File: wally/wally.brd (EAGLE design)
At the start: 5 x 8.6 mm, 28 parts, among them IC1 ESP32-S3-WROOM-1-N4, IC2 XTLV61048DBVR, J6 USBC, U1 RA-01H

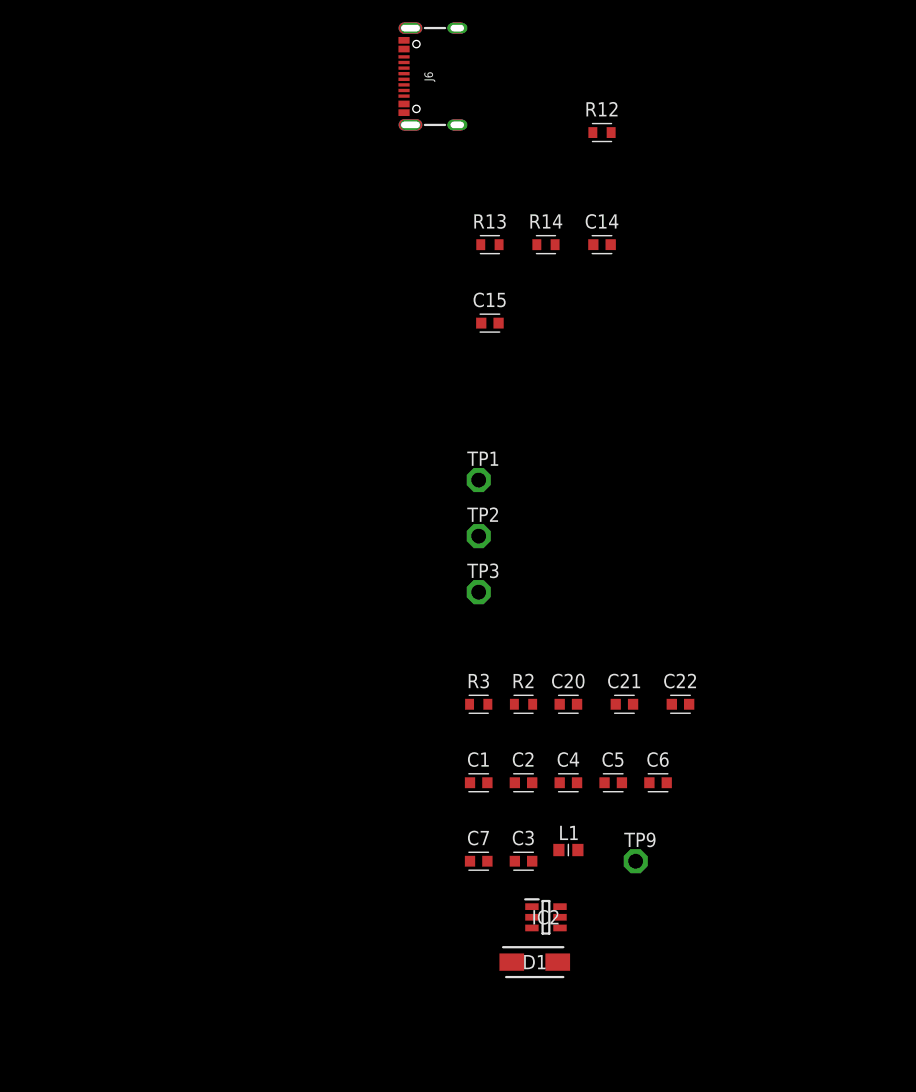
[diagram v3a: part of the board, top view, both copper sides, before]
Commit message: battery inputs
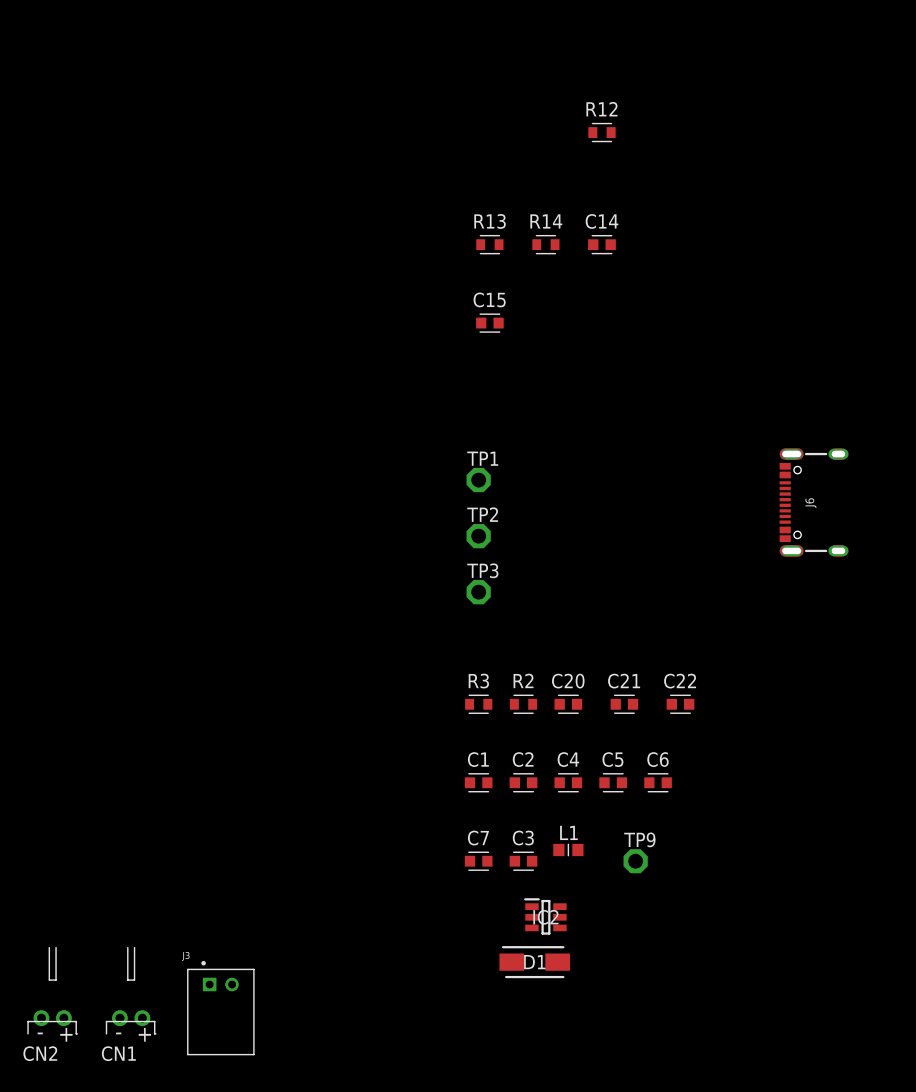
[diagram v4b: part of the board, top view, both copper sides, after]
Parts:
- added CN1, CN2: (no value), adafruit:JST-PH-2-THM-RA
- added J3: S2B-PH-K-S(LF)(SN), Connectors:S2B-PH-K-S(LF)(SN)
- moved J6 51.0 mm to (-24.0, -49.0)
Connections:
- net GND: now also CN1.2, CN2.2
- net VCC: now also CN1.1, CN2.1
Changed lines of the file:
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@@
 <wire x1="0" y1="0" x2="37" y2="0" width="0.254" layer="49"/>
 <wire x1="0" y1="0" x2="0" y2="-100" width="0.254" layer="49"/>
-<wire x1="37" y1="0" x2="36" y2="-1" width="0.254" layer="49"/>
-<wire x1="36" y1="-1" x2="36" y2="-100" width="0.254" layer="49"/>
-<wire x1="36" y1="-100" x2="0" y2="-100" width="0.254" layer="49"/>
+<wire x1="37" y1="0" x2="37" y2="-100" width="0.254" layer="49"/>
+<wire x1="37" y1="-100" x2="0" y2="-100" width="0.254" layer="49"/>
 </plain>
 <attributes>
@@
 <attribute name="VALUE" x="15" y="-67" size="1.27" layer="27" rot="R90" align="center"/>
 </element>
-<element name="J6" library="SparkFun-Connectors" package="USB-C-16P-2LAYER-PADS" override_package3d_urn="urn:adsk.eagle:package:44095805/2" override_package_urn="urn:adsk.eagle:footprint:44095806/1" value="USBC" x="-58" y="-11" smashed="yes" rot="R90">
-<attribute name="NAME" x="-55.46" y="-11" size="0.762" layer="25" rot="R90" align="center"/>
-<attribute name="PROD_ID" value="CONN-14122" x="-59" y="-11" size="1.778" layer="27" font="vector" ratio="15" rot="R90" display="off"/>
-<attribute name="VALUE" x="-54.19" y="-11" size="0.762" layer="27" rot="R90" align="center"/>
+<element name="J6" library="SparkFun-Connectors" package="USB-C-16P-2LAYER-PADS" override_package3d_urn="urn:adsk.eagle:package:44095805/2" override_package_urn="urn:adsk.eagle:footprint:44095806/1" value="USBC" x="-24" y="-49" smashed="yes" rot="R90">
+<attribute name="NAME" x="-21.46" y="-49" size="0.762" layer="25" rot="R90" align="center"/>
+<attribute name="PROD_ID" value="CONN-14122" x="-25" y="-49" size="1.778" layer="27" font="vector" ratio="15" rot="R90" display="off"/>
+<attribute name="VALUE" x="-20.19" y="-49" size="0.762" layer="27" rot="R90" align="center"/>
 </element>
 <element name="R12" library="Resistor" library_urn="urn:adsk.eagle:library:16378527" package="RESC1608X60" package3d_urn="urn:adsk.eagle:package:16378565/5" value="5k1" x="-40" y="-16" smashed="yes">
@@
 <attribute name="VALUE" x="-33" y="-68.4341" size="1.27" layer="27" align="top-center"/>
 <attribute name="VOLTAGE_RATING" value="" x="-54" y="-162" size="1.778" layer="27" font="vector" ratio="15" display="off"/>
+</element>
+<element name="J3" library="Connectors" library_urn="urn:adsk.eagle:library:28493002" package="S2B-PH-K-S(LF)(SN)" package3d_urn="urn:adsk.eagle:package:10989924/2" value="S2B-PH-K-S(LF)(SN)" x="-74" y="-92" smashed="yes">
+<attribute name="CREATED_BY" value="PCBLayout.com" x="-74" y="-92" size="1.778" layer="27" font="vector" ratio="15" display="off"/>
+<attribute name="DIGI_KEY_PART_NUMBER" value="455-1719-ND" x="-74" y="-92" size="1.778" layer="27" font="vector" ratio="15" display="off"/>
+<attribute name="MANUFACTURER" value="JST Sales America Inc." x="-74" y="-92" size="1.778" layer="27" font="vector" ratio="15" display="off"/>
+<attribute name="MPN" value="S2B-PH-K-S(LF)(SN)" x="-74" y="-92" size="1.778" layer="27" font="vector" ratio="15" display="off"/>
+<attribute name="NAME" x="-77.429" y="-89.714" size="0.6096" layer="25"/>
+<attribute name="VALUE" x="-77.3" y="-99.2" size="0.6096" layer="27"/>
+</element>
+<element name="CN1" library="adafruit" library_urn="urn:adsk.eagle:library:420" package="JST-PH-2-THM-RA" package3d_urn="urn:adsk.eagle:package:6240694/1" value="" x="-82" y="-95" smashed="yes">
+<attribute name="NAME" x="-84.7" y="-98.8" size="1.27" layer="25" font="vector"/>
+</element>
+<element name="CN2" library="adafruit" library_urn="urn:adsk.eagle:library:420" package="JST-PH-2-THM-RA" package3d_urn="urn:adsk.eagle:package:6240694/1" value="" x="-89" y="-95" smashed="yes">
+<attribute name="NAME" x="-91.7" y="-98.8" size="1.27" layer="25" font="vector"/>
 </element>
 </elements>
@@
 <contactref element="C3" pad="2"/>
 <contactref element="IC2" pad="6"/>
+<contactref element="CN1" pad="2"/>
+<contactref element="CN2" pad="2"/>
+<wire x1="-83" y1="-95" x2="-90" y2="-95" width="0" layer="19" extent="1-1"/>
+<wire x1="-51.7746" y1="-81" x2="-83" y2="-95" width="0" layer="19" extent="1-1"/>
 <wire x1="-46.2254" y1="-81" x2="-51.7746" y2="-81" width="0" layer="19" extent="1-1"/>
 <wire x1="-43.75" y1="-85.05" x2="-46.2254" y2="-81" width="0" layer="19" extent="1-1"/>
@@
 <wire x1="-33.7746" y1="-67" x2="-38.7746" y2="-67" width="0" layer="19" extent="1-1"/>
 <wire x1="-51" y1="-57" x2="-50.1848" y2="-67" width="0" layer="19" extent="1-1"/>
+<wire x1="-23.66" y1="-52.225" x2="-33.7746" y2="-67" width="0" layer="19" extent="1-1"/>
+<wire x1="-23.66" y1="-45.775" x2="-23.66" y2="-52.225" width="0" layer="19" extent="1-1"/>
 <wire x1="-50.7746" y1="-33" x2="-51" y2="-57" width="0" layer="19" extent="1-1"/>
 <wire x1="-49.1848" y1="-26" x2="-50.7746" y2="-33" width="0" layer="19" extent="1-1"/>
@@
 <wire x1="-40.7746" y1="-26" x2="-44.1848" y2="-26" width="0" layer="19" extent="1-1"/>
 <wire x1="-39.1848" y1="-16" x2="-40.7746" y2="-26" width="0" layer="19" extent="1-1"/>
-<wire x1="-57.66" y1="-14.225" x2="-49.1848" y2="-26" width="0" layer="19" extent="1-1"/>
-<wire x1="-57.66" y1="-7.775" x2="-57.66" y2="-14.225" width="0" layer="19" extent="1-1"/>
-<wire x1="3" y1="-15.42" x2="-39.1848" y2="-16" width="0" layer="19" extent="1-1"/>
-<wire x1="3" y1="-28.12" x2="3" y2="-15.42" width="0" layer="19" extent="1-1"/>
+<wire x1="3" y1="-28.12" x2="-23.66" y2="-45.775" width="0" layer="19" extent="1-1"/>
+<wire x1="3" y1="-15.42" x2="3" y2="-28.12" width="0" layer="19" extent="1-1"/>
 <wire x1="9.49" y1="-58.25" x2="3" y2="-28.12" width="0" layer="19" extent="1-1"/>
 <wire x1="15.81" y1="-67.1" x2="9.49" y2="-58.25" width="0" layer="19" extent="1-1"/>
@@
 <contactref element="J6" pad="SHLD3"/>
 <contactref element="R13" pad="1"/>
-<wire x1="-52.905" y1="-15.318" x2="-50.8152" y2="-26" width="0" layer="19" extent="1-1"/>
-<wire x1="-57.085" y1="-15.318" x2="-52.905" y2="-15.318" width="0" layer="19" extent="1-1"/>
-<wire x1="-52.905" y1="-6.682" x2="-52.905" y2="-15.318" width="0" layer="19" extent="1-1"/>
-<wire x1="-57.085" y1="-6.682" x2="-52.905" y2="-6.682" width="0" layer="19" extent="1-1"/>
+<wire x1="-18.905" y1="-53.318" x2="-50.8152" y2="-26" width="0" layer="19" extent="1-1"/>
+<wire x1="-23.085" y1="-53.318" x2="-18.905" y2="-53.318" width="0" layer="19" extent="1-1"/>
+<wire x1="-18.905" y1="-44.682" x2="-18.905" y2="-53.318" width="0" layer="19" extent="1-1"/>
+<wire x1="-23.085" y1="-44.682" x2="-18.905" y2="-44.682" width="0" layer="19" extent="1-1"/>
 </signal>
 <signal name="N$24">
 <contactref element="J6" pad="B5"/>
 <contactref element="R12" pad="1"/>
-<wire x1="-40.8152" y1="-16" x2="-57.66" y2="-9.25" width="0" layer="19" extent="1-1"/>
+<wire x1="-40.8152" y1="-16" x2="-23.66" y2="-47.25" width="0" layer="19" extent="1-1"/>
 </signal>
 <signal name="N$25">
 <contactref element="J6" pad="A5"/>
 <contactref element="R14" pad="1"/>
-<wire x1="-57.66" y1="-12.25" x2="-45.8152" y2="-26" width="0" layer="19" extent="1-1"/>
+<wire x1="-23.66" y1="-50.25" x2="-45.8152" y2="-26" width="0" layer="19" extent="1-1"/>
 </signal>
 <signal name="N$26">
@@
 <contactref element="J6" pad="A6"/>
 <contactref element="J6" pad="B6"/>
-<wire x1="-57.66" y1="-10.25" x2="-57.66" y2="-11.25" width="0" layer="19" extent="1-1"/>
+<wire x1="-23.66" y1="-48.25" x2="-23.66" y2="-49.25" width="0" layer="19" extent="1-1"/>
 </signal>
 <signal name="USB_D-">
 <contactref element="J6" pad="A7"/>
 <contactref element="J6" pad="B7"/>
-<wire x1="-57.66" y1="-10.75" x2="-57.66" y2="-11.75" width="0" layer="19" extent="1-1"/>
+<wire x1="-23.66" y1="-48.75" x2="-23.66" y2="-49.75" width="0" layer="19" extent="1-1"/>
 </signal>
 <signal name="RXD">
@@
 <contactref element="C21" pad="2"/>
 <contactref element="C20" pad="2"/>
-<wire x1="-43.75" y1="-86" x2="-43.75" y2="-86.95" width="0" layer="19" extent="1-1"/>
-<wire x1="-42.15" y1="-80" x2="-43.75" y2="-86" width="0" layer="19" extent="1-1"/>
+<contactref element="CN2" pad="1"/>
+<contactref element="CN1" pad="1"/>
+<wire x1="-81" y1="-95" x2="-88" y2="-95" width="0" layer="19" extent="1-1"/>
+<wire x1="-50.2254" y1="-81" x2="-81" y2="-95" width="0" layer="19" extent="1-1"/>
+<wire x1="-51.7746" y1="-74" x2="-50.2254" y2="-81" width="0" layer="19" extent="1-1"/>
+<wire x1="-42.15" y1="-80" x2="-50.2254" y2="-81" width="0" layer="19" extent="1-1"/>
 <wire x1="-42.2254" y1="-74" x2="-42.15" y2="-80" width="0" layer="19" extent="1-1"/>
 <wire x1="-38.2254" y1="-74" x2="-42.2254" y2="-74" width="0" layer="19" extent="1-1"/>
 <wire x1="-34.2254" y1="-74" x2="-38.2254" y2="-74" width="0" layer="19" extent="1-1"/>
+<wire x1="-43.75" y1="-86" x2="-42.15" y2="-80" width="0" layer="19" extent="1-1"/>
+<wire x1="-43.75" y1="-86.95" x2="-43.75" y2="-86" width="0" layer="19" extent="1-1"/>
 <wire x1="-42.2254" y1="-67" x2="-42.2254" y2="-74" width="0" layer="19" extent="1-1"/>
 <wire x1="-37.2254" y1="-67" x2="-42.2254" y2="-67" width="0" layer="19" extent="1-1"/>
 <wire x1="-32.2254" y1="-67" x2="-37.2254" y2="-67" width="0" layer="19" extent="1-1"/>
-<wire x1="-50.2254" y1="-81" x2="-42.15" y2="-80" width="0" layer="19" extent="1-1"/>
-<wire x1="-51.7746" y1="-74" x2="-50.2254" y2="-81" width="0" layer="19" extent="1-1"/>
 </signal>
 <signal name="N$2">

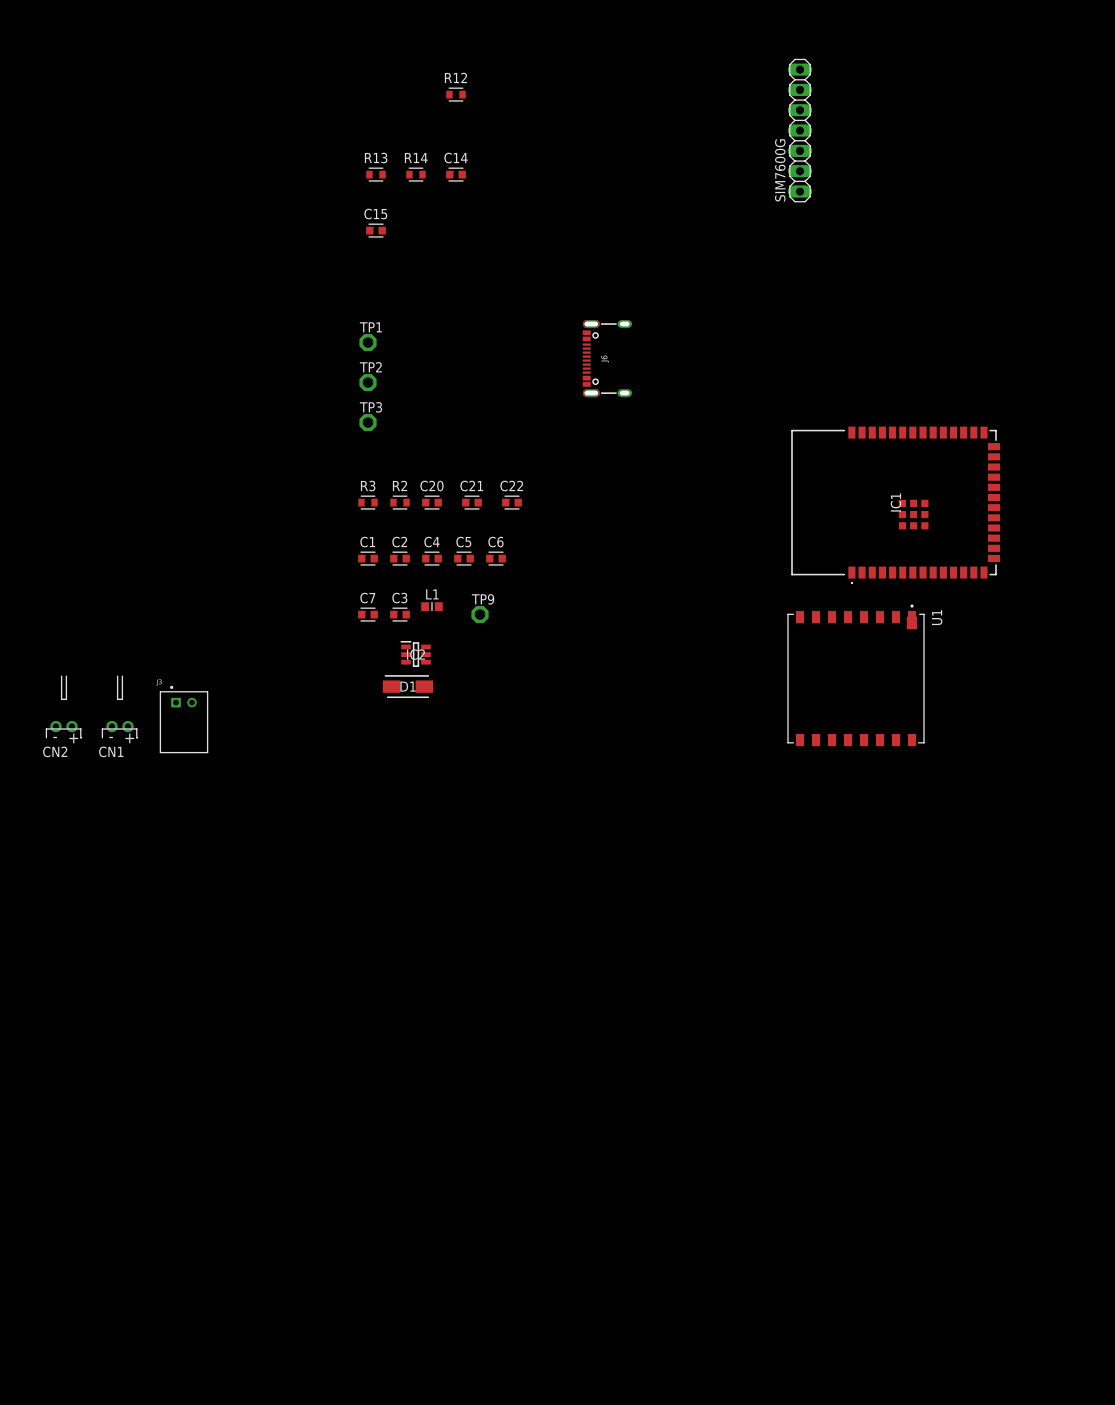
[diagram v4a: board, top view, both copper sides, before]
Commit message: LDO for 3v3
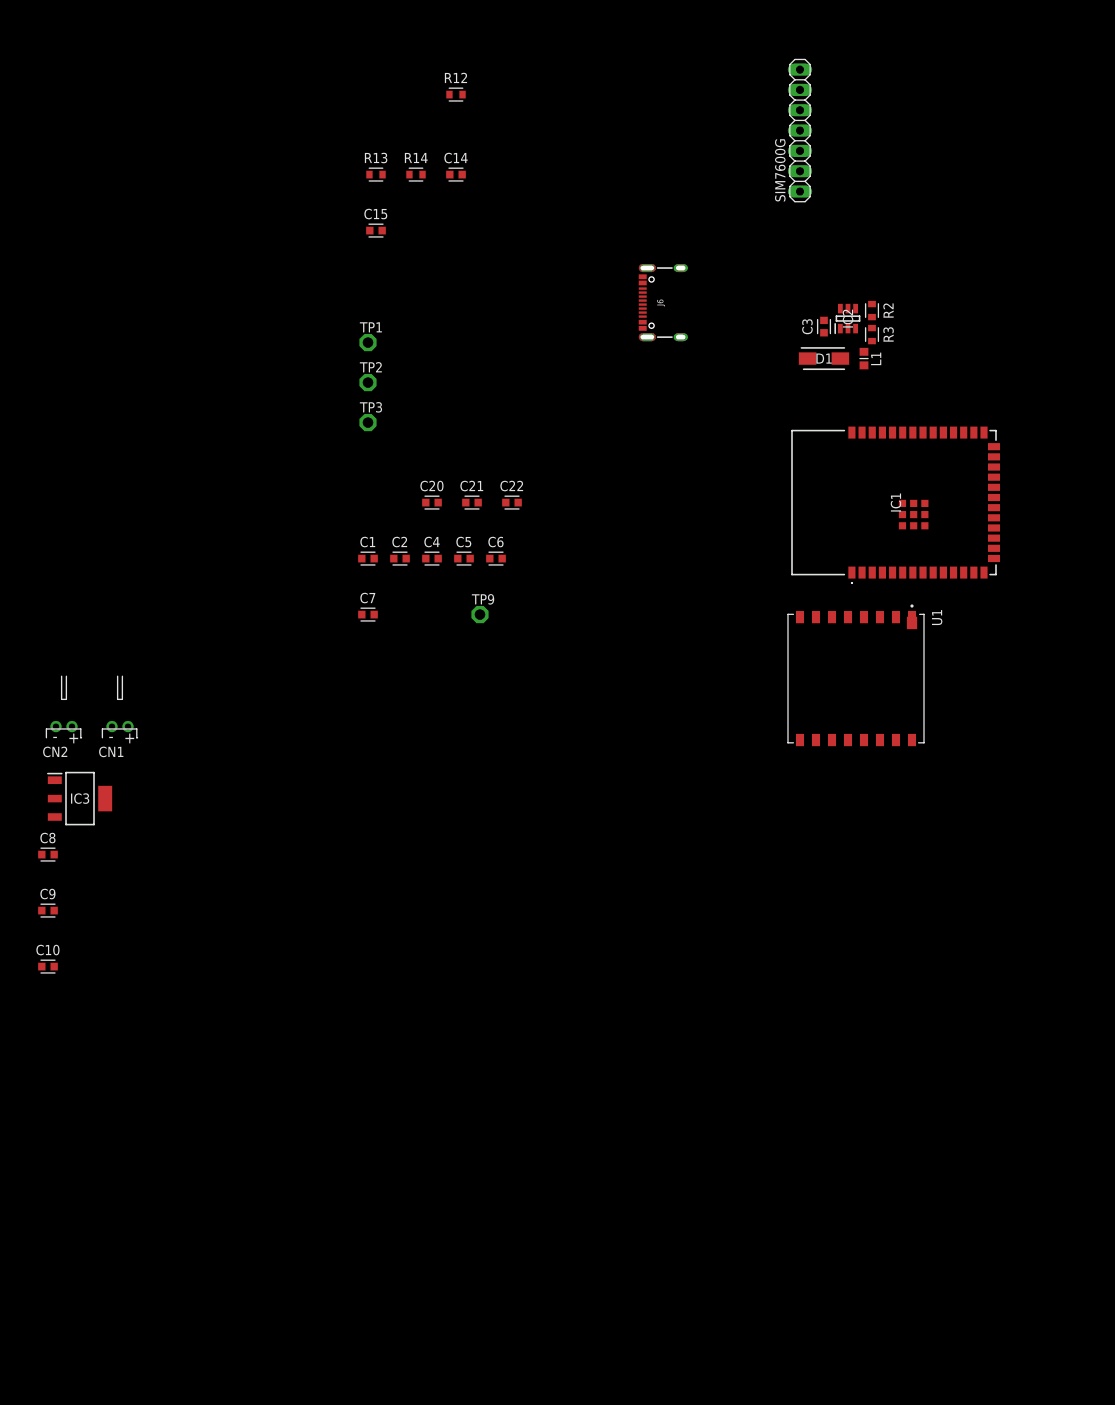
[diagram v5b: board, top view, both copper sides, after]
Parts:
- removed J3: S2B-PH-K-S(LF)(SN), Connectors:S2B-PH-K-S(LF)(SN)
- added C10, C8: 1u, Capacitor:CAPC1608X85
- added C9: 100n, Capacitor:CAPC1608X85
- added IC3: TLV1117LV33DCYR, SamacSys_Parts:SOT230P700X180-4N
- moved IC2 68.4 mm to (9.00, -44.0), turned to 90 degrees
- moved R3 66.4 mm to (12.0, -46.0), turned to 270 degrees
- moved D1 66.2 mm to (6.00, -49.0)
- moved C3 64.1 mm to (6.00, -45.0), turned to 90 degrees
- moved R2 63.7 mm to (12.0, -43.0), turned to 270 degrees
- moved L1 62.3 mm to (11.0, -49.0), turned to 270 degrees
- moved J6 9.90 mm to (-17.0, -42.0)
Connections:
- net 3V3: now also C10.1, IC3.2, IC3.4
- net GND: now also C10.2, C8.2, C9.2, IC3.1
- net N$26: now also J6.VBUS1, J6.VBUS2
- net VCC: now also C8.1, C9.1, IC3.3
